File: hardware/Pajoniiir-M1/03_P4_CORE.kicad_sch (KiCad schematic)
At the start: 42 parts, among them U1 ESP32-P4NRW32X, U3 TLV62569DRLR

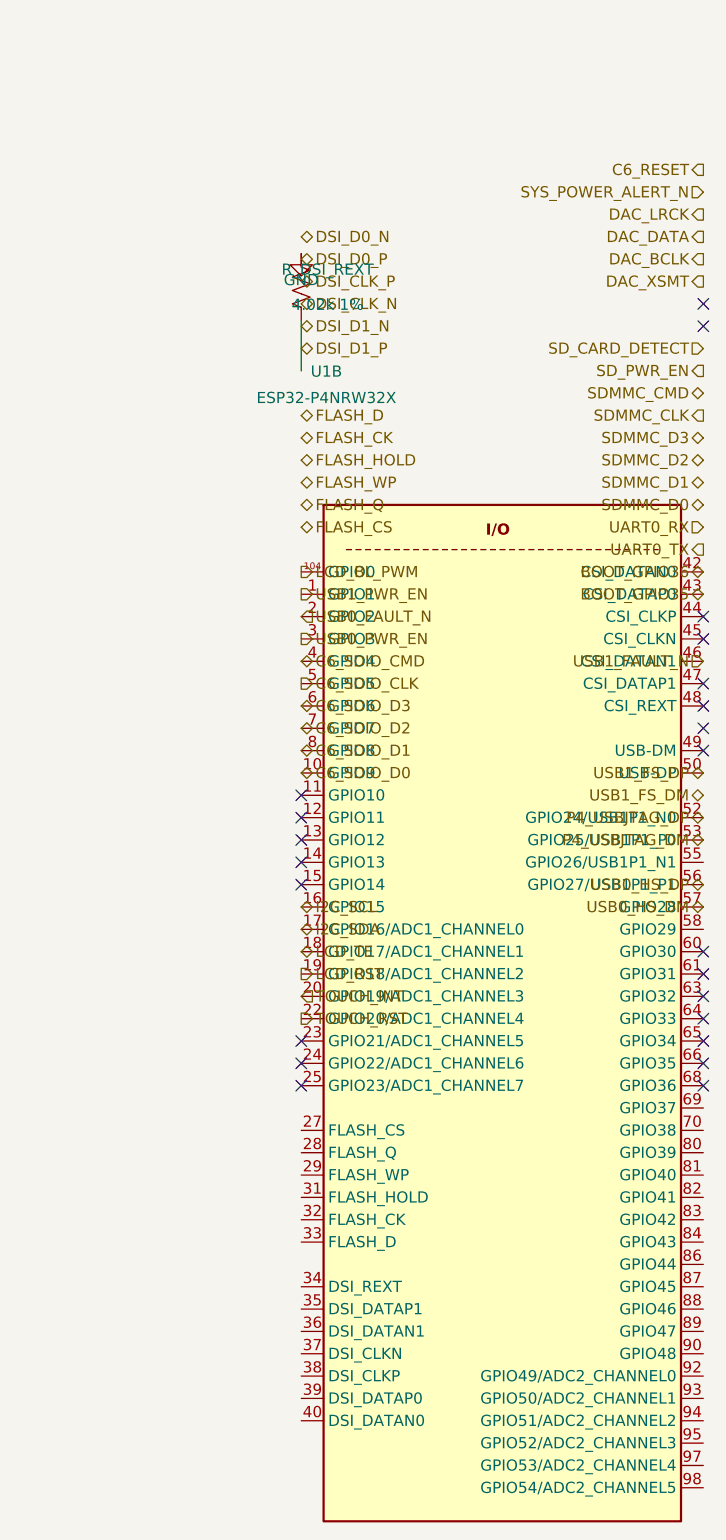
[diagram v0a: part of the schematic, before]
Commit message: hardware: correct P4 unit-2 pin coordinate mapping
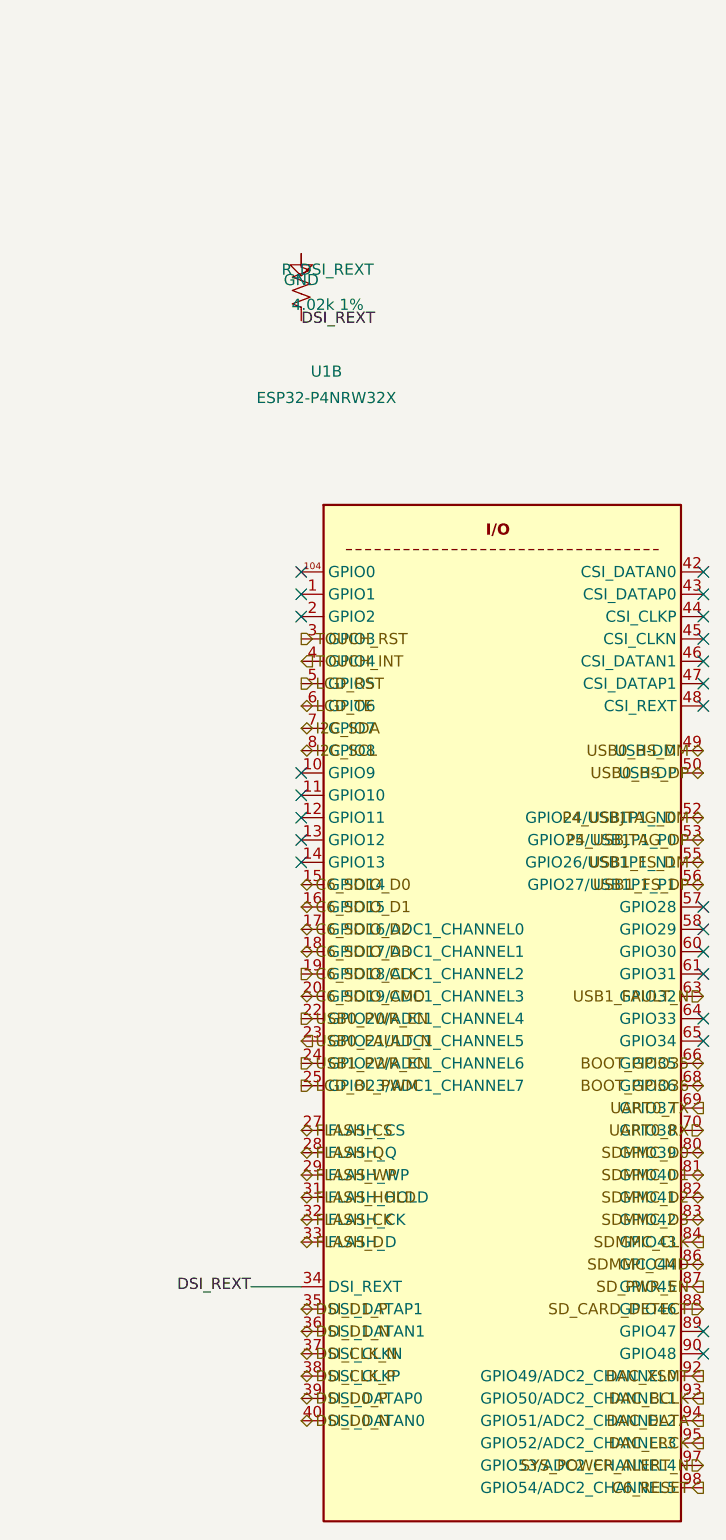
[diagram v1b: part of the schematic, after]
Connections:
- net BOOT_GPIO35: now also U1.66 (GPIO35); no longer U1.43 (CSI_DATAP0)
- net BOOT_GPIO36: now also U1.68 (GPIO36); no longer U1.42 (CSI_DATAN0)
- net C6_RESET: now also U1.98 (GPIO54/ADC2_CHANNEL5)
- net C6_SDIO_CLK: now also U1.19 (GPIO18/ADC1_CHANNEL2); no longer U1.5 (GPIO5)
- net C6_SDIO_CMD: now also U1.20 (GPIO19/ADC1_CHANNEL3); no longer U1.4 (GPIO4)
- net C6_SDIO_D0: now also U1.15 (GPIO14); no longer U1.10 (GPIO9)
- net C6_SDIO_D1: now also U1.16 (GPIO15); no longer U1.8 (GPIO8)
- net C6_SDIO_D2: now also U1.17 (GPIO16/ADC1_CHANNEL0); no longer U1.7 (GPIO7)
- net C6_SDIO_D3: now also U1.18 (GPIO17/ADC1_CHANNEL1); no longer U1.6 (GPIO6)
- net DAC_BCLK: now also U1.93 (GPIO50/ADC2_CHANNEL1)
- net DAC_DATA: now also U1.94 (GPIO51/ADC2_CHANNEL2)
- net DAC_LRCK: now also U1.95 (GPIO52/ADC2_CHANNEL3)
- net DAC_XSMT: now also U1.92 (GPIO49/ADC2_CHANNEL0)
- net DSI_CLK_N: now also U1.37 (DSI_CLKN)
- net DSI_CLK_P: now also U1.38 (DSI_CLKP)
- net DSI_D0_N: now also U1.40 (DSI_DATAN0)
- net DSI_D0_P: now also U1.39 (DSI_DATAP0)
- net DSI_D1_N: now also U1.36 (DSI_DATAN1); no longer R_DSI_REXT.2
- net FLASH_CK: now also U1.32 (FLASH_CK)
- net FLASH_CS: now also U1.27 (FLASH_CS)
- net FLASH_D: now also U1.33 (FLASH_D)
- net FLASH_HOLD: now also U1.31 (FLASH_HOLD)
- net FLASH_Q: now also U1.28 (FLASH_Q)
- net FLASH_WP: now also U1.29 (FLASH_WP)
- net I2C_SCL: now also U1.8 (GPIO8); no longer U1.16 (GPIO15)
- net I2C_SDA: now also U1.7 (GPIO7); no longer U1.17 (GPIO16/ADC1_CHANNEL0)
- net LCD_BL_PWM: now also U1.25 (GPIO23/ADC1_CHANNEL7); no longer U1.104 (GPIO0)
- net LCD_RST: now also U1.5 (GPIO5); no longer U1.19 (GPIO18/ADC1_CHANNEL2)
- net LCD_TE: now also U1.6 (GPIO6); no longer U1.18 (GPIO17/ADC1_CHANNEL1)
- net P4_USBJTAG_DM: now also U1.52 (GPIO24/USB1P1_N0); no longer U1.53 (GPIO25/USB1P1_P0)
- net P4_USBJTAG_DP: now also U1.53 (GPIO25/USB1P1_P0); no longer U1.52 (GPIO24/USB1P1_N0)
- net SDMMC_CLK: now also U1.84 (GPIO43)
- net SDMMC_CMD: now also U1.86 (GPIO44)
- net SDMMC_D0: now also U1.80 (GPIO39)
- net SDMMC_D1: now also U1.81 (GPIO40)
- net SDMMC_D2: now also U1.82 (GPIO41)
- net SDMMC_D3: now also U1.83 (GPIO42)
- net SD_CARD_DETECT: now also U1.88 (GPIO46)
- net SD_PWR_EN: now also U1.87 (GPIO45)
- net SYS_POWER_ALERT_N: now also U1.97 (GPIO53/ADC2_CHANNEL4)
- net TOUCH_INT: now also U1.4 (GPIO4); no longer U1.20 (GPIO19/ADC1_CHANNEL3)
- net TOUCH_RST: now also U1.3 (GPIO3); no longer U1.22 (GPIO20/ADC1_CHANNEL4)
- net UART0_RX: now also U1.70 (GPIO38)
- net UART0_TX: now also U1.69 (GPIO37)
- net USB0_FAULT_N: now also U1.23 (GPIO21/ADC1_CHANNEL5); no longer U1.2 (GPIO2)
- net USB0_HS_DM: now also U1.49 (USB-DM); no longer U1.57 (GPIO28)
- net USB0_HS_DP: now also U1.50 (USB-DP); no longer U1.56 (GPIO27/USB1P1_P1)
- net USB0_PWR_EN: now also U1.22 (GPIO20/ADC1_CHANNEL4); no longer U1.3 (GPIO3)
- net USB1_FAULT_N: now also U1.63 (GPIO32); no longer U1.46 (CSI_DATAN1)
- net USB1_FS_DM: now also U1.55 (GPIO26/USB1P1_N1)
- net USB1_FS_DP: now also U1.56 (GPIO27/USB1P1_P1); no longer U1.50 (USB-DP)
- net USB1_PWR_EN: now also U1.24 (GPIO22/ADC1_CHANNEL6); no longer U1.1 (GPIO1)
- net DSI_REXT: now reaches U1.34 (DSI_REXT)
- net DSI_REXT: now also R_DSI_REXT.2
- net DSI_D1_P: now reaches U1.35 (DSI_DATAP1)

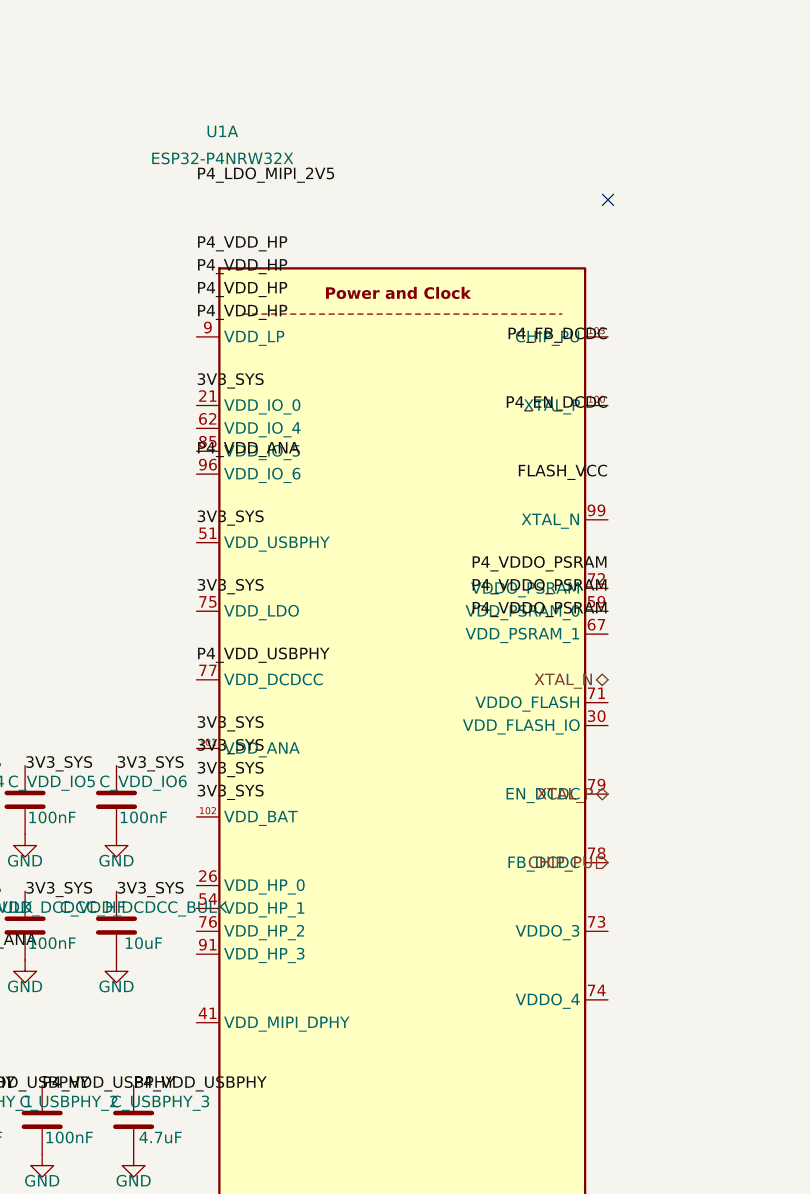
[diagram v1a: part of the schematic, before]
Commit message: hardware: correct P4 unit-1 pin coordinate mapping
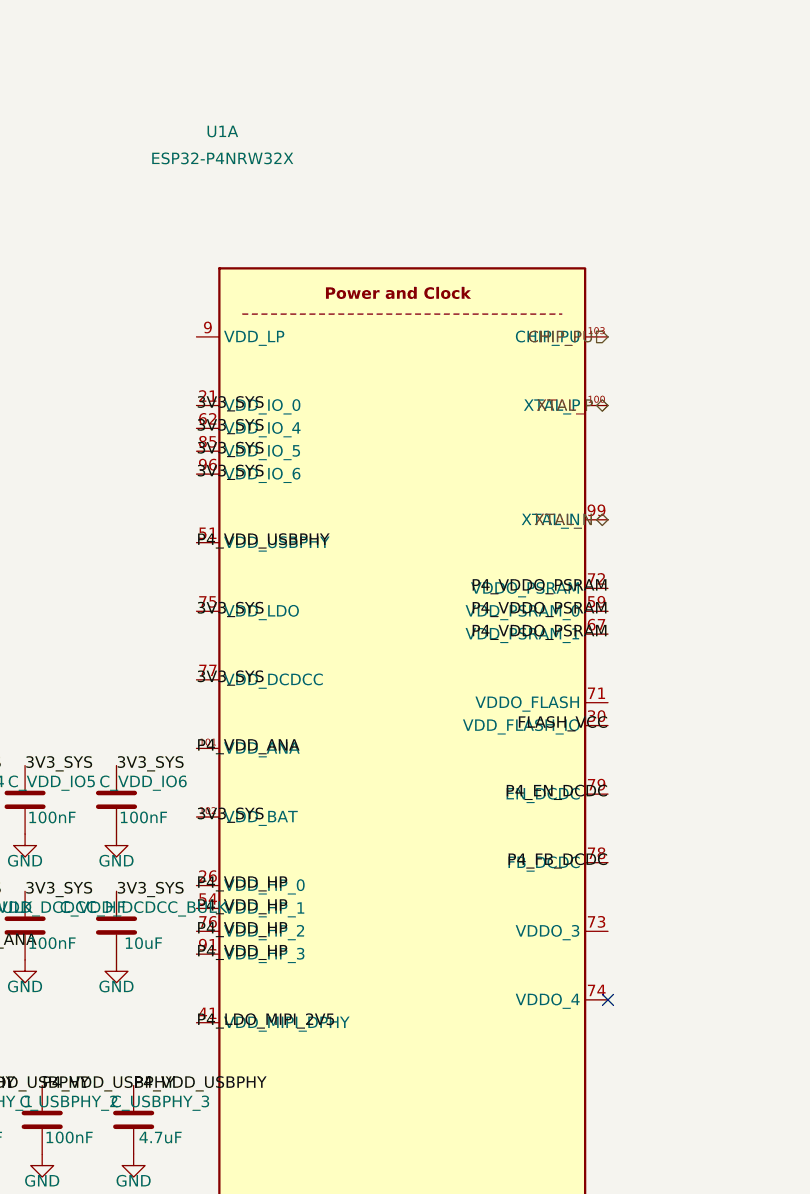
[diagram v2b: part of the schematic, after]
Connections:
- net 3V3_SYS: now also U1.102 (VDD_BAT), U1.21 (VDD_IO_0), U1.62 (VDD_IO_4), U1.75 (VDD_LDO), U1.77 (VDD_DCDCC), U1.85 (VDD_IO_5), U1.96 (VDD_IO_6); no longer U1.101 (VDD_ANA)
- net CHIP_PU: now also U1.103 (CHIP_PU); no longer U1.78 (FB_DCDC)
- net FLASH_VCC: now also U1.30 (VDD_FLASH_IO)
- net P4_EN_DCDC: now also U1.79 (EN_DCDC); no longer U1.100 (XTAL_P)
- net P4_FB_DCDC: now also U1.78 (FB_DCDC); no longer U1.103 (CHIP_PU)
- net P4_LDO_MIPI_2V5: now also U1.41 (VDD_MIPI_DPHY)
- net P4_VDDO_PSRAM: now also U1.67 (VDD_PSRAM_1)
- net P4_VDD_ANA: now also U1.101 (VDD_ANA); no longer U1.85 (VDD_IO_5)
- net P4_VDD_HP: now also U1.26 (VDD_HP_0), U1.54 (VDD_HP_1), U1.76 (VDD_HP_2), U1.91 (VDD_HP_3)
- net P4_VDD_USBPHY: now also U1.51 (VDD_USBPHY)
- net XTAL_N: now also U1.99 (XTAL_N)
- net XTAL_P: now also U1.100 (XTAL_P); no longer U1.79 (EN_DCDC)
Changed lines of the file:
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@@
   (hierarchical_label "SYS_POWER_ALERT_N" (shape input) (at 353.06 290.195 180) (effects (font (size 1.27 1.27))))
   (hierarchical_label "C6_RESET" (shape output) (at 353.06 292.735 180) (effects (font (size 1.27 1.27))))
-  (hierarchical_label "XTAL_N" (shape bidirectional) (at 134.62 120.65 180) (effects (font (size 1.27 1.27))))
-  (hierarchical_label "XTAL_P" (shape bidirectional) (at 134.62 133.35 180) (effects (font (size 1.27 1.27))))
-  (hierarchical_label "CHIP_PU" (shape input) (at 134.62 140.97 180) (effects (font (size 1.27 1.27))))
+  (hierarchical_label "XTAL_N" (shape bidirectional) (at 134.62 102.87 180) (effects (font (size 1.27 1.27))))
+  (hierarchical_label "XTAL_P" (shape bidirectional) (at 134.62 90.17 180) (effects (font (size 1.27 1.27))))
+  (hierarchical_label "CHIP_PU" (shape input) (at 134.62 82.55 180) (effects (font (size 1.27 1.27))))
   (symbol
     (lib_id "Device:R_US") (at 307.34 156.21 0) (unit 1)
@@
     (instances (project "Pajoniiir-M1" (path "/2c8dd352-b7b8-4d9e-8f93-5dd43be2a100/31000003-6b2a-4a3a-8c91-000000000003" (reference "#PWR0301") (unit 1))))
   )
-  (label "3V3_SYS" (at 88.9 133.35 0) (effects (font (size 1.27 1.27))))
-  (label "3V3_SYS" (at 88.9 130.81 0) (effects (font (size 1.27 1.27))))
-  (label "3V3_SYS" (at 88.9 128.27 0) (effects (font (size 1.27 1.27))))
-  (label "3V3_SYS" (at 88.9 125.73 0) (effects (font (size 1.27 1.27))))
-  (label "3V3_SYS" (at 88.9 87.63 0) (effects (font (size 1.27 1.27))))
-  (label "3V3_SYS" (at 88.9 110.49 0) (effects (font (size 1.27 1.27))))
-  (label "3V3_SYS" (at 88.9 102.87 0) (effects (font (size 1.27 1.27))))
-  (label "P4_VDD_ANA" (at 88.9 95.25 0) (effects (font (size 1.27 1.27))))
+  (label "3V3_SYS" (at 88.9 90.17 0) (effects (font (size 1.27 1.27))))
+  (label "3V3_SYS" (at 88.9 92.71 0) (effects (font (size 1.27 1.27))))
+  (label "3V3_SYS" (at 88.9 95.25 0) (effects (font (size 1.27 1.27))))
+  (label "3V3_SYS" (at 88.9 97.79 0) (effects (font (size 1.27 1.27))))
+  (label "3V3_SYS" (at 88.9 135.89 0) (effects (font (size 1.27 1.27))))
+  (label "3V3_SYS" (at 88.9 113.03 0) (effects (font (size 1.27 1.27))))
+  (label "3V3_SYS" (at 88.9 120.65 0) (effects (font (size 1.27 1.27))))
+  (label "P4_VDD_ANA" (at 88.9 128.27 0) (effects (font (size 1.27 1.27))))
   (symbol
     (lib_id "Device:R_US") (at 50.165 149.86 90) (unit 1)
@@
     (instances (project "Pajoniiir-M1" (path "/2c8dd352-b7b8-4d9e-8f93-5dd43be2a100/31000003-6b2a-4a3a-8c91-000000000003" (reference "#PWR0302") (unit 1))))
   )
-  (label "P4_VDD_HP" (at 88.9 80.01 0) (effects (font (size 1.27 1.27))))
-  (label "P4_VDD_HP" (at 88.9 77.47 0) (effects (font (size 1.27 1.27))))
-  (label "P4_VDD_HP" (at 88.9 74.93 0) (effects (font (size 1.27 1.27))))
-  (label "P4_VDD_HP" (at 88.9 72.39 0) (effects (font (size 1.27 1.27))))
-  (label "P4_VDD_USBPHY" (at 88.9 118.11 0) (effects (font (size 1.27 1.27))))
+  (label "P4_VDD_HP" (at 88.9 143.51 0) (effects (font (size 1.27 1.27))))
+  (label "P4_VDD_HP" (at 88.9 146.05 0) (effects (font (size 1.27 1.27))))
+  (label "P4_VDD_HP" (at 88.9 148.59 0) (effects (font (size 1.27 1.27))))
+  (label "P4_VDD_HP" (at 88.9 151.13 0) (effects (font (size 1.27 1.27))))
+  (label "P4_VDD_USBPHY" (at 88.9 105.41 0) (effects (font (size 1.27 1.27))))
   (symbol
     (lib_id "Device:R_US") (at 50.165 165.735 90) (unit 1)
@@
     (instances (project "Pajoniiir-M1" (path "/2c8dd352-b7b8-4d9e-8f93-5dd43be2a100/31000003-6b2a-4a3a-8c91-000000000003" (reference "#PWR0392") (unit 1))))
   )
-  (label "FLASH_VCC" (at 134.62 97.79 180) (effects (font (size 1.27 1.27))))
+  (label "FLASH_VCC" (at 134.62 125.73 180) (effects (font (size 1.27 1.27))))
   (hierarchical_label "FLASH_VCC" (shape output) (at 168.275 36.195 0) (effects (font (size 1.27 1.27))))
   (symbol
@@
     (instances (project "Pajoniiir-M1" (path "/2c8dd352-b7b8-4d9e-8f93-5dd43be2a100/31000003-6b2a-4a3a-8c91-000000000003" (reference "#PWR0321") (unit 1))))
   )
+  (label "P4_VDDO_PSRAM" (at 134.62 110.49 180) (effects (font (size 1.27 1.27))))
   (label "P4_VDDO_PSRAM" (at 134.62 113.03 180) (effects (font (size 1.27 1.27))))
-  (label "P4_VDDO_PSRAM" (at 134.62 110.49 180) (effects (font (size 1.27 1.27))))
-  (label "P4_VDDO_PSRAM" (at 134.62 107.95 180) (effects (font (size 1.27 1.27))))
+  (label "P4_VDDO_PSRAM" (at 134.62 115.57 180) (effects (font (size 1.27 1.27))))
   (symbol
     (lib_id "Device:C") (at 189.865 40.005 0) (unit 1)
@@
     (instances (project "Pajoniiir-M1" (path "/2c8dd352-b7b8-4d9e-8f93-5dd43be2a100/31000003-6b2a-4a3a-8c91-000000000003" (reference "#PWR033230") (unit 1))))
   )
-  (label "P4_LDO_MIPI_2V5" (at 88.9 64.77 0) (effects (font (size 1.27 1.27))))
+  (label "P4_LDO_MIPI_2V5" (at 88.9 158.75 0) (effects (font (size 1.27 1.27))))
   (hierarchical_label "P4_LDO_MIPI_2V5" (shape output) (at 250.19 36.195 0) (effects (font (size 1.27 1.27))))
   (symbol
@@
     (instances (project "Pajoniiir-M1" (path "/2c8dd352-b7b8-4d9e-8f93-5dd43be2a100/31000003-6b2a-4a3a-8c91-000000000003" (reference "#PWR034270") (unit 1))))
   )
-  (no_connect (at 134.62 67.31))
+  (no_connect (at 134.62 156.21))
   (symbol
     (lib_id "power:GND") (at 111.76 30.48 0) (unit 1)
@@
   )
   (label "P4_EN_DCDC" (at 202.565 90.17 0) (effects (font (size 1.27 1.27))))
-  (label "P4_EN_DCDC" (at 134.62 90.17 180) (effects (font (size 1.27 1.27))))
+  (label "P4_EN_DCDC" (at 134.62 133.35 180) (effects (font (size 1.27 1.27))))
   (symbol
     (lib_id "power:GND") (at 210.185 97.79 0) (unit 1)
@@
   )
   (label "P4_FB_DCDC" (at 217.805 90.17 0) (effects (font (size 1.27 1.27))))
-  (label "P4_FB_DCDC" (at 134.62 82.55 180) (effects (font (size 1.27 1.27))))
+  (label "P4_FB_DCDC" (at 134.62 140.97 180) (effects (font (size 1.27 1.27))))
   (symbol
     (lib_id "Device:R_US") (at 250.19 92.71 0) (unit 1)
